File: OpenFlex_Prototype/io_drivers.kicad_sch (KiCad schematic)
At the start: 29 parts, among them Q1 STP80NF55-08, Q2 STP80NF55-08, Q3 STP80NF55-08, Q4 STP80NF55-08, U2 LM324, U3 TC4424, U4 TC4424

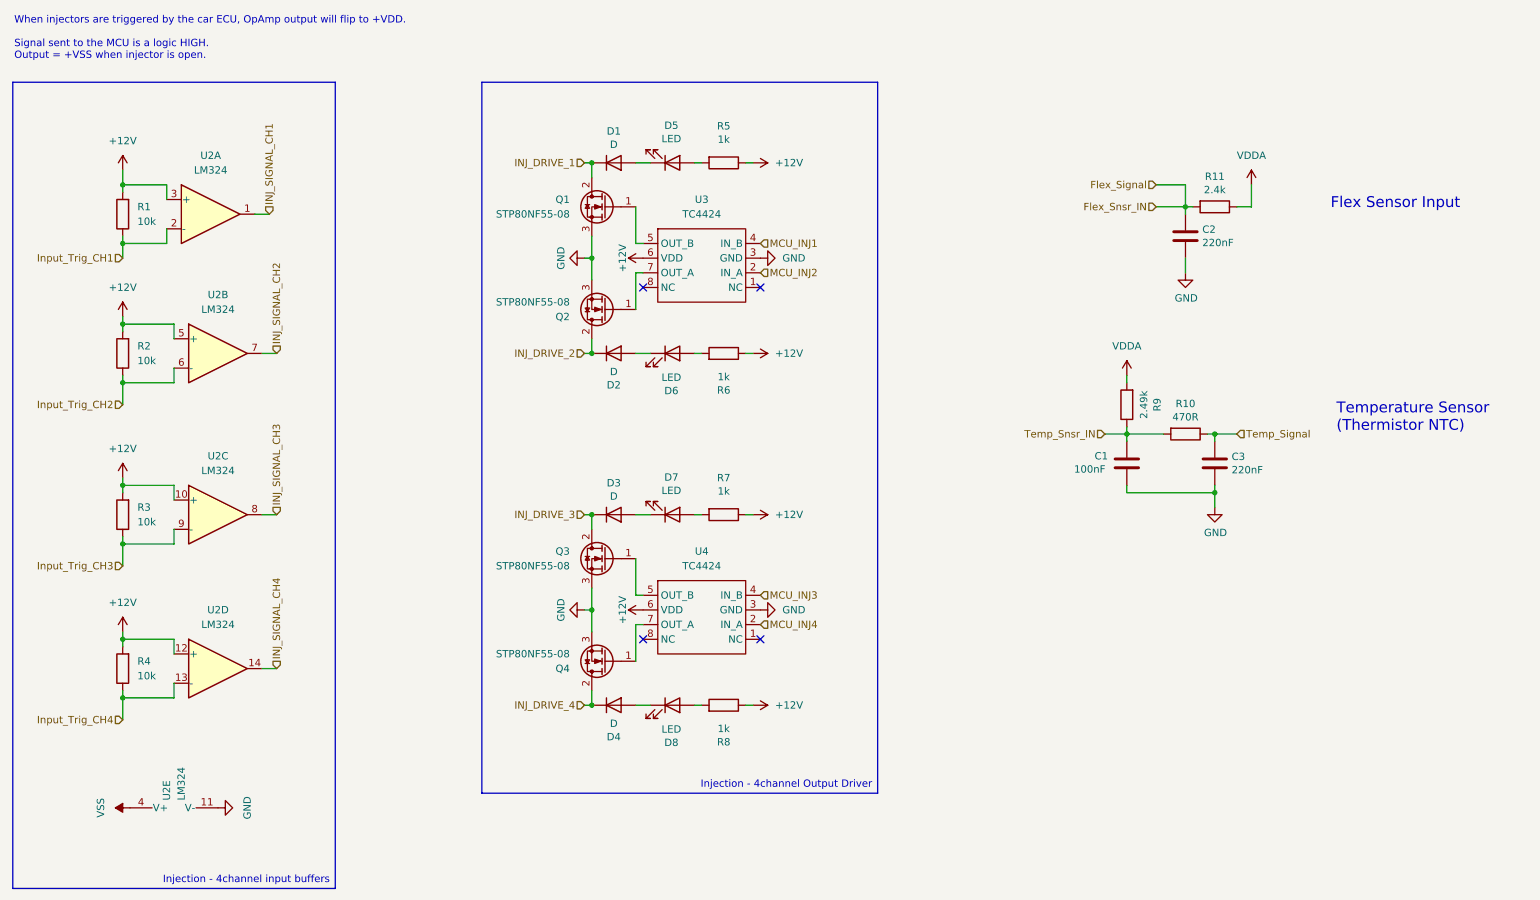
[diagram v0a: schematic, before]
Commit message: BOM Updated with thermistor. Enclosure in progress
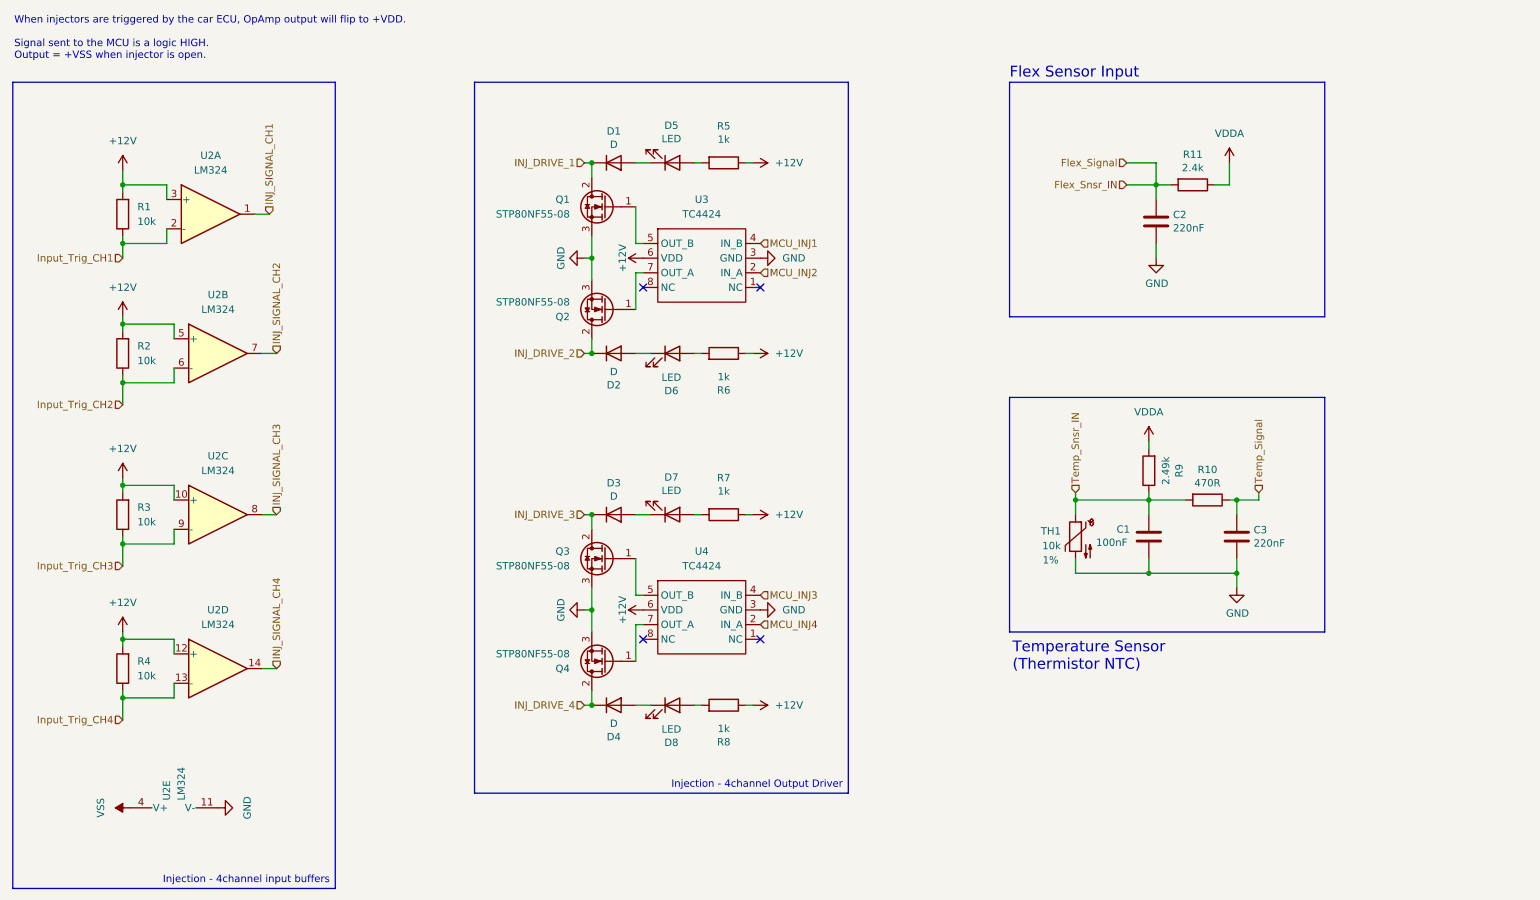
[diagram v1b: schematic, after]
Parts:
- added TH1: 10k, symbol Device:Thermistor_NTC
- R9: Digikey_Part_Number (none) -> 738-RNF14BTE2K49CT-ND; Manufacturer_Name Yageo -> Stackpole Electronics Inc; Manufacturer_Part_Number MFR-25FBF52-2K49 -> RNF14BTE2K49; Mouser_Part_Number 603-MFR-25FBF52-2K49 -> (none); URL https://www.mouser.fr/ProductDetail/YAGEO/MFR-25FBF52-2K49?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 -> https://www.digikey.fr/fr/products/detail/stackpole-electro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; URL_Digikey (none) -> https://www.digikey.fr/fr/products/detail/stackpole-electro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
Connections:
- net GND: now also TH1.2
- net Temp_Snsr_IN: now also TH1.1
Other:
- moved on the sheet: C1, C2, C3, R10, R11, R9
